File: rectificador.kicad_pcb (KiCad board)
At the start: 4 copper layers, 134 parts, among them J1 TRIF, J10 AC_FASE_2, J11 AC_FASE_3, J12 SEC, J13 BOB_CONT, J14 PUENTE_P, J15 PUENTE_N, J16 RES_LIM, J17 CONTACT, J18 INDUCT, J19 MCU, J2 CHASIS, J21 VENT, J22 TC, J3 PRIM, J4 FILTRO_1, J5 FILTRO_2, J6 FILTRO_3, J7 BUS, J8 COM, J9 AC_FASE_1, K1 SRD-05VDC-SLC, Q1 2n2222, Q2 MMBT3904, U1 LM7805_TO220, U2 PC817, U3 PC817, U4 ACS712xLCTR-30A, U5 AMC1301, U6 LM358, U7 MAX6675, U8 220VAC_5VD_SWITCHING, U9 PC817

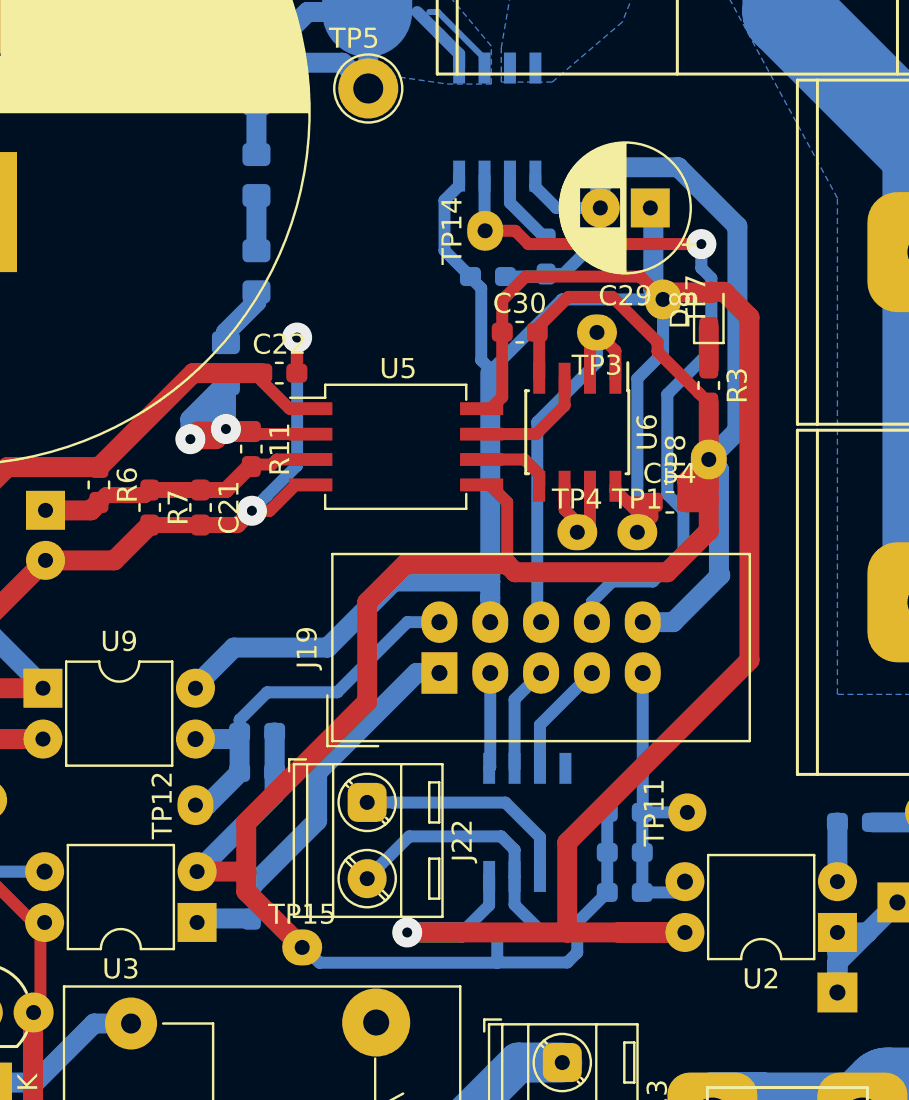
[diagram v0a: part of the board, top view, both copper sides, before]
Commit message: actualizo valores de componentes
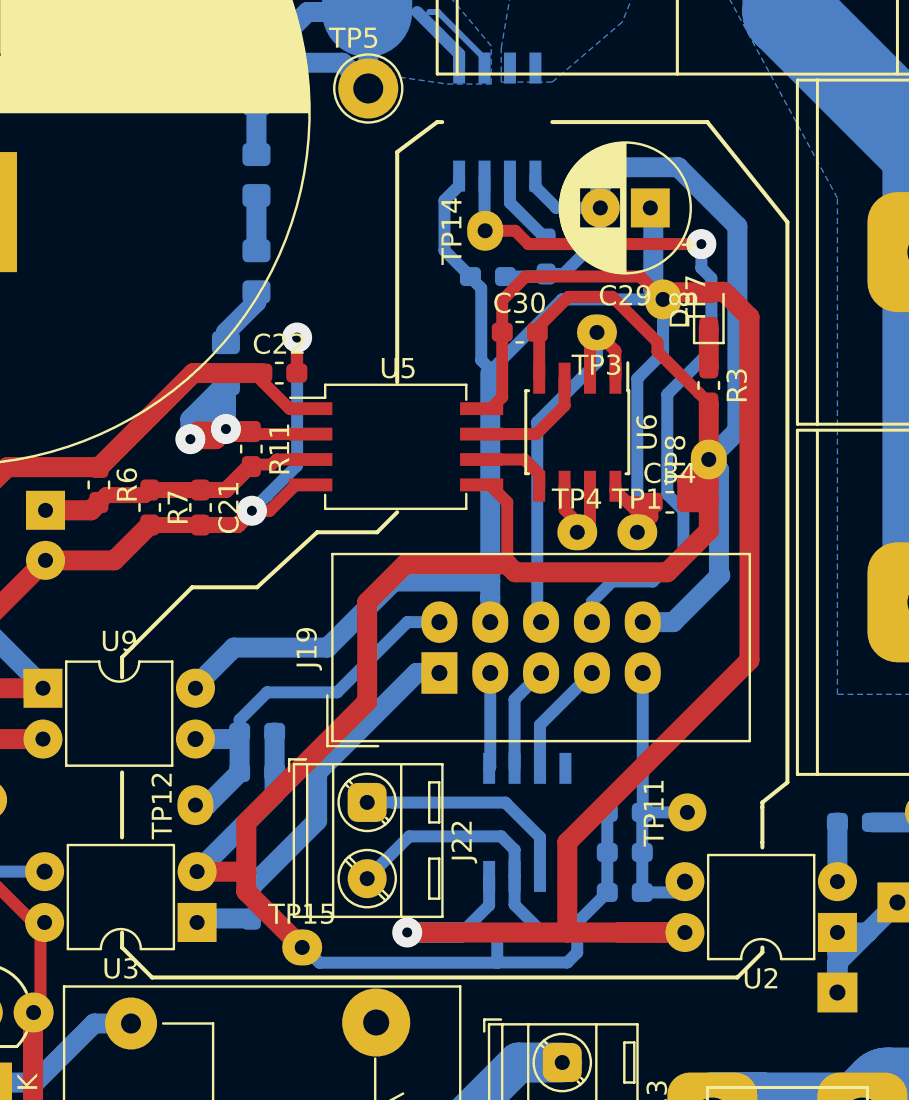
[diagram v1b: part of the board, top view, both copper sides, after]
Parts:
- C19: value 10uF/10V -> 47uF/25V
- C29: value 10uFx10V -> 47uFx25V
- C31: value 47uFx25V -> 47uFx25V/NP
- D10: value 2V4 -> 2V4/NP
- D5: value LED_NA -> LED_AZ
- JP1: value MCU/AUTO -> MCU/AUTO-NP
- Q2: value MMBT3904 -> MMBT3904/NP
- R12: value 1K -> 1K/NP
- R19: value 1K -> NP
- R2: value 470 -> 470/NP
- R5: value 390 -> 220
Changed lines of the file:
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@@
   (general
     (thickness 1.6)
-    (drawings 5)
+    (drawings 27)
     (tracks 787)
     (zones 0)
@@
       (effects (font (size 1 1) (thickness 0.15)))
     )
-    (fp_text value 1K (at 0 1.43) (layer F.Fab)
+    (fp_text value NP (at 0 1.43) (layer F.Fab)
       (effects (font (size 1 1) (thickness 0.15)))
     )
@@
       (effects (font (size 1 1) (thickness 0.15)))
     )
-    (fp_text value 470 (at 0 1.43) (layer F.Fab)
+    (fp_text value 470/NP (at 0 1.43) (layer F.Fab)
       (effects (font (size 1 1) (thickness 0.15)))
     )
@@
       (effects (font (size 1 1) (thickness 0.15)) (justify mirror))
     )
-    (fp_text value 390 (at 0 -1.43 270) (layer B.Fab)
+    (fp_text value 220 (at 0 -1.43 270) (layer B.Fab)
       (effects (font (size 1 1) (thickness 0.15)) (justify mirror))
     )
@@
       (effects (font (size 1 1) (thickness 0.15)))
     )
-    (fp_text value LED_NA (at 0 1.43 90) (layer F.Fab)
+    (fp_text value LED_AZ (at 0 1.43 90) (layer F.Fab)
       (effects (font (size 1 1) (thickness 0.15)))
     )
@@
       (effects (font (size 1 1) (thickness 0.15)))
     )
-    (fp_text value MMBT3904 (at 0 2.5) (layer F.Fab)
+    (fp_text value MMBT3904/NP (at 0 2.5) (layer F.Fab)
       (effects (font (size 1 1) (thickness 0.15)))
     )
@@
       (effects (font (size 1 1) (thickness 0.15)))
     )
-    (fp_text value 1K (at 0 1.43) (layer F.Fab)
+    (fp_text value 1K/NP (at 0 1.43) (layer F.Fab)
       (effects (font (size 1 1) (thickness 0.15)))
     )
@@
       (effects (font (size 1 1) (thickness 0.15)))
     )
-    (fp_text value 2V4 (at 3.81 2.12) (layer F.Fab)
+    (fp_text value 2V4/NP (at 3.81 2.12) (layer F.Fab)
       (effects (font (size 1 1) (thickness 0.15)))
     )
@@
       (effects (font (size 1 1) (thickness 0.15)))
     )
-    (fp_text value MCU/AUTO (at 0 7.41) (layer F.Fab)
+    (fp_text value MCU/AUTO-NP (at 0 7.41) (layer F.Fab)
       (effects (font (size 1 1) (thickness 0.15)))
     )
@@
       (effects (font (size 1 1) (thickness 0.15)) (justify mirror))
     )
-    (fp_text value 10uF/10V (at 1.25 -4.4 270) (layer B.Fab)
+    (fp_text value 47uF/25V (at 1.25 -4.4 270) (layer B.Fab)
       (effects (font (size 1 1) (thickness 0.15)) (justify mirror))
     )
@@
       (effects (font (size 1 1) (thickness 0.15)))
     )
-    (fp_text value 10uFx10V (at 1.25 4.4 180) (layer F.Fab)
+    (fp_text value 47uFx25V (at 1.25 4.4 180) (layer F.Fab)
       (effects (font (size 1 1) (thickness 0.15)))
     )
@@
       (effects (font (size 1 1) (thickness 0.15)))
     )
-    (fp_text value 47uFx25V (at 1.25 4.4 180) (layer F.Fab)
+    (fp_text value 47uFx25V/NP (at 1.25 4.4 180) (layer F.Fab)
       (effects (font (size 1 1) (thickness 0.15)))
     )
@@
     )
   )
+  (gr_line (start 134.25 143) (end 134.25 142.75) (layer F.SilkS) (width 0.2))
+  (gr_line (start 109 124.75) (end 112 122) (layer F.SilkS) (width 0.2))
+  (gr_line (start 105.75 124.75) (end 109 124.75) (layer F.SilkS) (width 0.2))
+  (gr_line (start 102.25 128.25) (end 105.75 124.75) (layer F.SilkS) (width 0.2))
+  (gr_line (start 102.25 129.25) (end 102.25 128.25) (layer F.SilkS) (width 0.2))
+  (gr_line (start 116 114.5) (end 116 103) (layer F.SilkS) (width 0.2))
+  (gr_line (start 112 122) (end 115 122) (layer F.SilkS) (width 0.2))
+  (gr_line (start 116 121) (end 115 122) (layer F.SilkS) (width 0.2))
+  (gr_line (start 123.75 101.5) (end 131.5 101.5) (layer F.SilkS) (width 0.2))
+  (gr_line (start 118 101.5) (end 118.25 101.5) (layer F.SilkS) (width 0.2))
+  (gr_line (start 135.5 134.5) (end 135.5 106.5) (layer F.SilkS) (width 0.2))
+  (gr_line (start 134.25 135.5) (end 135.5 134.5) (layer F.SilkS) (width 0.2))
+  (gr_line (start 134.25 135.75) (end 134.25 135.5) (layer F.SilkS) (width 0.2))
+  (gr_line (start 134.25 137.5) (end 134.25 135.75) (layer F.SilkS) (width 0.2))
+  (gr_line (start 134.25 137.5) (end 134.25 137.75) (layer F.SilkS) (width 0.2))
+  (gr_line (start 133 144.25) (end 134.25 143) (layer F.SilkS) (width 0.2))
+  (gr_line (start 103.75 144.25) (end 133 144.25) (layer F.SilkS) (width 0.2))
+  (gr_line (start 102.25 142.75) (end 103.75 144.25) (layer F.SilkS) (width 0.2))
+  (gr_line (start 102.25 142) (end 102.25 142.75) (layer F.SilkS) (width 0.2))
+  (gr_line (start 102.25 134) (end 102.25 137.25) (layer F.SilkS) (width 0.2))
+  (gr_line (start 116 103) (end 118 101.5) (layer F.SilkS) (width 0.2))
+  (gr_line (start 131.5 101.5) (end 135.5 106.5) (layer F.SilkS) (width 0.2))
   (gr_text "PUENTE_TRIFASICO\nFIUBA-LABCATYP\n2019-JUN-08-AR" (at 220 150) (layer F.Cu)
     (effects (font (size 1.3 1) (thickness 0.2)))
